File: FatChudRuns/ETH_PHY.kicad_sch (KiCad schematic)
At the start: 1 part, among them U2 DP83848I

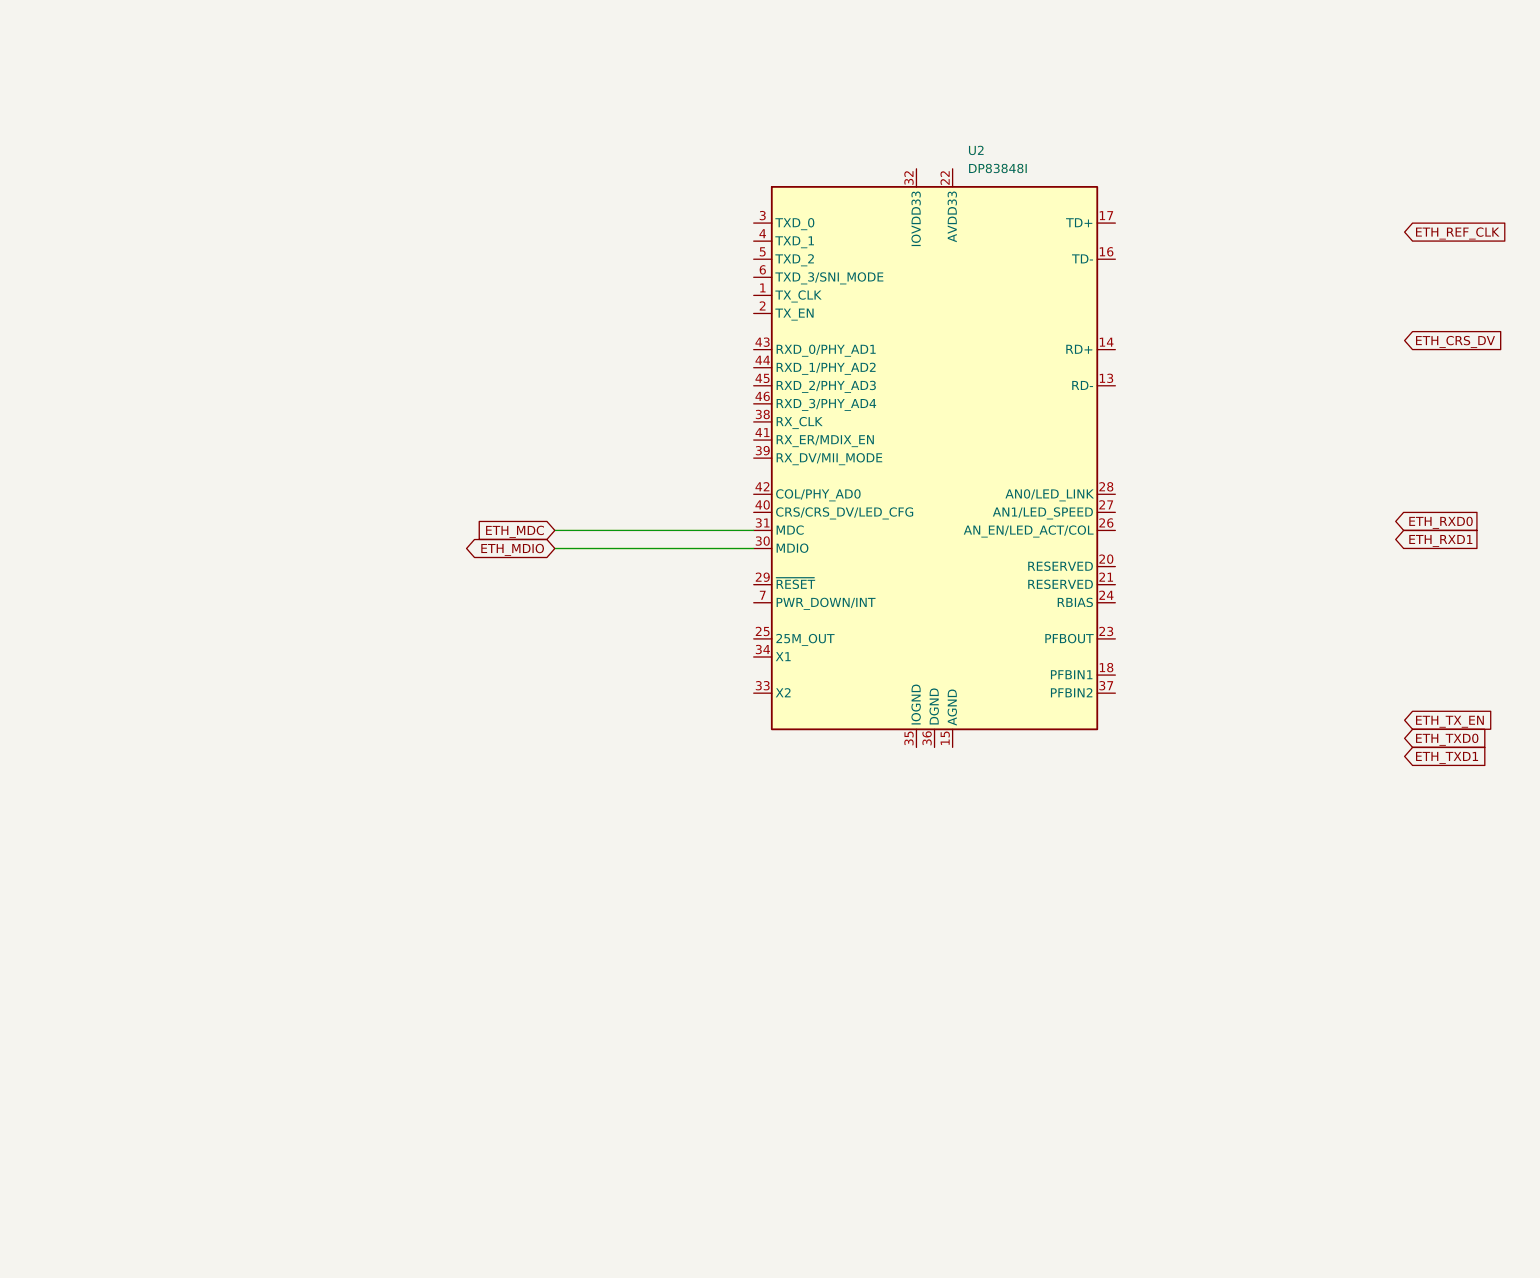
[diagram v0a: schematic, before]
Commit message: connected phy to uC and added strapping options
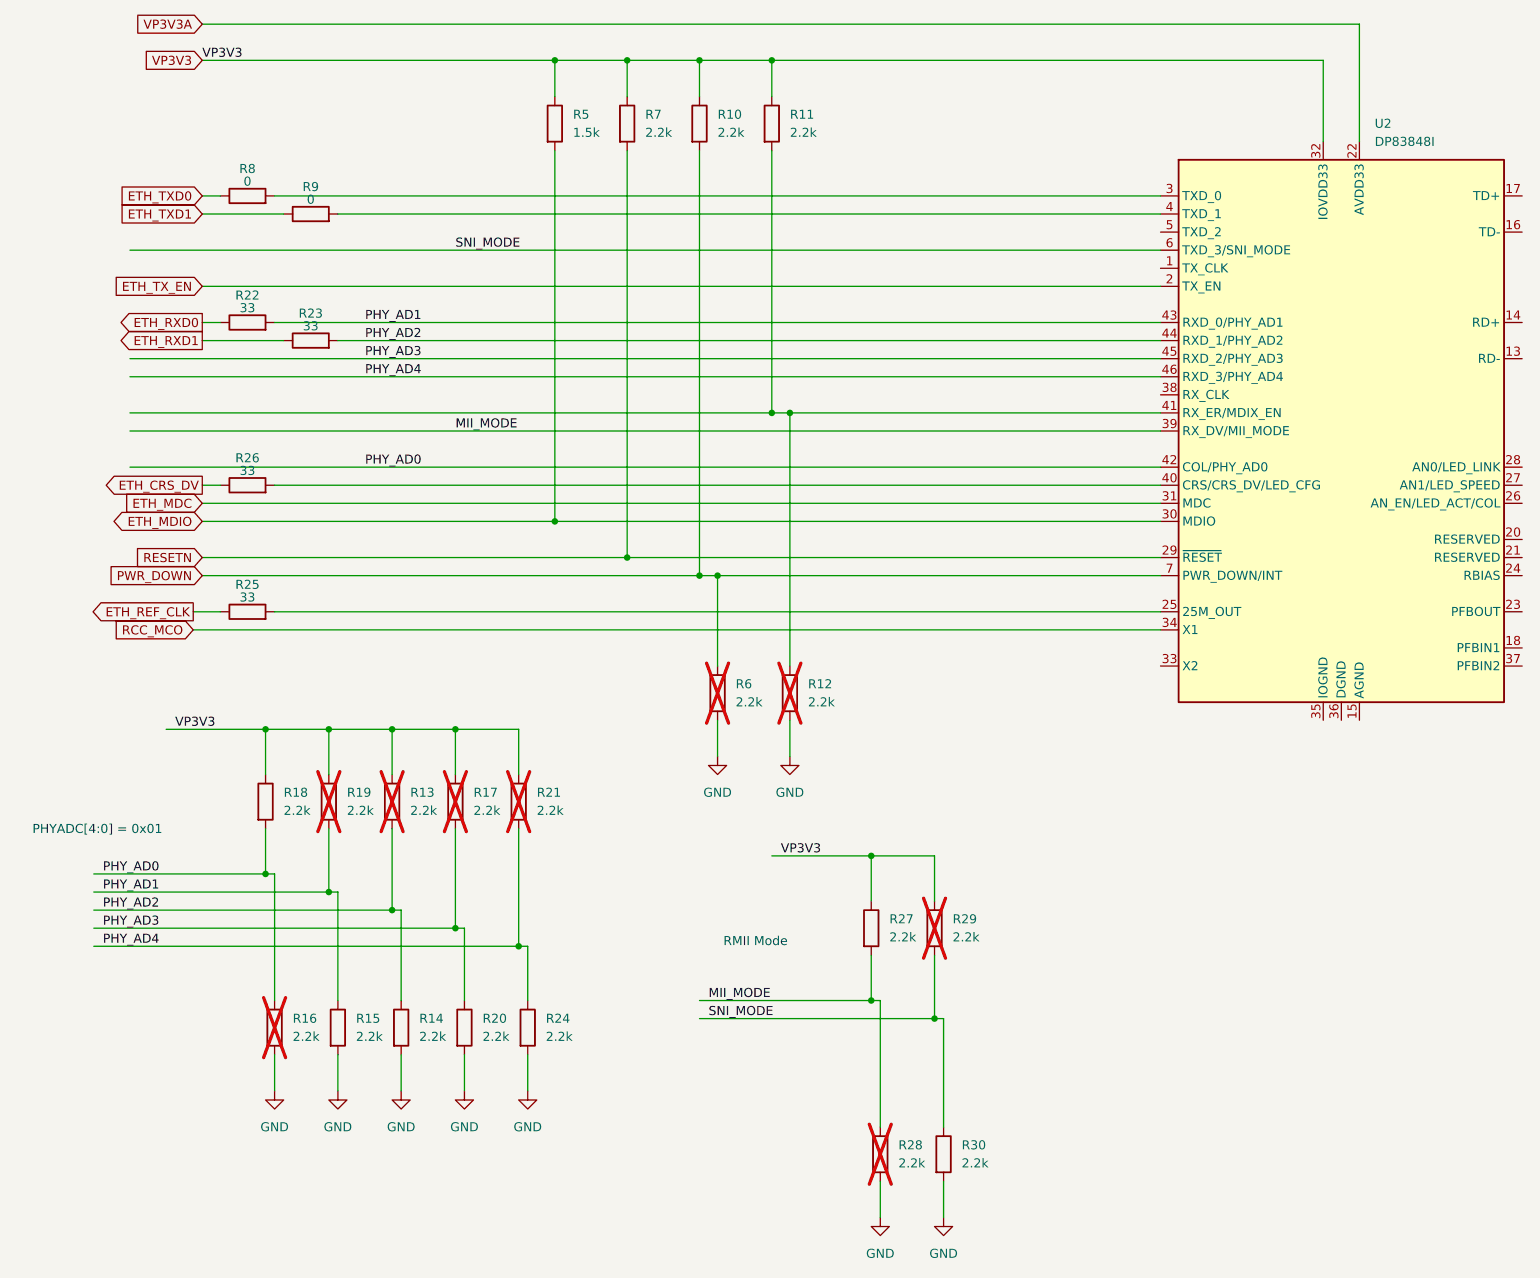
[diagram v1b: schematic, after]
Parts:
- added R10, R11, R12, R13, R14, R15, R16, R17, R18, R19, R20, R21, R24, R27, R28, R29, R30, R6, R7: 2.2k, Resistor_SMD:R_0603_1608Metric, symbol Device:R
- added R22, R23, R25, R26: 33, Resistor_SMD:R_0603_1608Metric, symbol Device:R
- added R5: 1.5k, Resistor_SMD:R_0603_1608Metric, symbol Device:R
- added R8, R9: 0, Resistor_SMD:R_0603_1608Metric, symbol Device:R
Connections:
- net ETH_CRS_DV: now also R26.1
- net ETH_MDIO: now also R5.2
- net ETH_REF_CLK: now also R25.1
- net ETH_RXD0: now also R22.1
- net ETH_RXD1: now also R23.1
- net ETH_TXD0: now also R8.1
- net ETH_TXD1: now also R9.1
- net ETH_TX_EN: now also U2.2 (TX_EN)
- net VP3V3A: now reaches U2.22 (AVDD33)
- net at U2.25 (25M_OUT): now also R25.2
- net RESETN: now reaches U2.29 (~{RESET})
- net RESETN: now also R7.2
- net at U2.3 (TXD_0): now also R8.2
- net VP3V3: now reaches U2.32 (IOVDD33), U2.48 (IOVDD33)
- net VP3V3: now also R10.1, R11.1, R13.1, R17.1, R18.1, R19.1, R21.1, R27.1, R29.1, R5.1, R7.1
- net RCC_MCO: now reaches U2.34 (X1)
- net MII_MODE: now reaches U2.39 (RX_DV/MII_MODE)
- net MII_MODE: now also R27.2, R28.1
- net at U2.4 (TXD_1): now also R9.2
- net at U2.40 (CRS/CRS_DV/LED_CFG): now also R26.2
- net at U2.41 (RX_ER/MDIX_EN): now also R11.2, R12.1
- net PHY_AD0: now reaches U2.42 (COL/PHY_AD0)
- net PHY_AD0: now also R16.1, R18.2
- net PHY_AD1: now reaches U2.43 (RXD_0/PHY_AD1)
- net PHY_AD1: now also R15.1, R19.2, R22.2
- net PHY_AD2: now reaches U2.44 (RXD_1/PHY_AD2)
- net PHY_AD2: now also R13.2, R14.1, R23.2
- net PHY_AD3: now reaches U2.45 (RXD_2/PHY_AD3)
- net PHY_AD3: now also R17.2, R20.1
- net PHY_AD4: now reaches U2.46 (RXD_3/PHY_AD4)
- net PHY_AD4: now also R21.2, R24.1
- net SNI_MODE: now reaches U2.6 (TXD_3/SNI_MODE)
- net SNI_MODE: now also R29.2, R30.1
- net PWR_DOWN: now reaches U2.7 (PWR_DOWN/INT)
- net PWR_DOWN: now also R10.2, R6.1
- new net GND: R12.2, R14.2, R15.2, R16.2, R20.2, R24.2, R28.2, R30.2, R6.2
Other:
- note added: "PHYADC[4:0] = 0x01"
- note added: "RMII Mode"
- moved on the sheet: U2

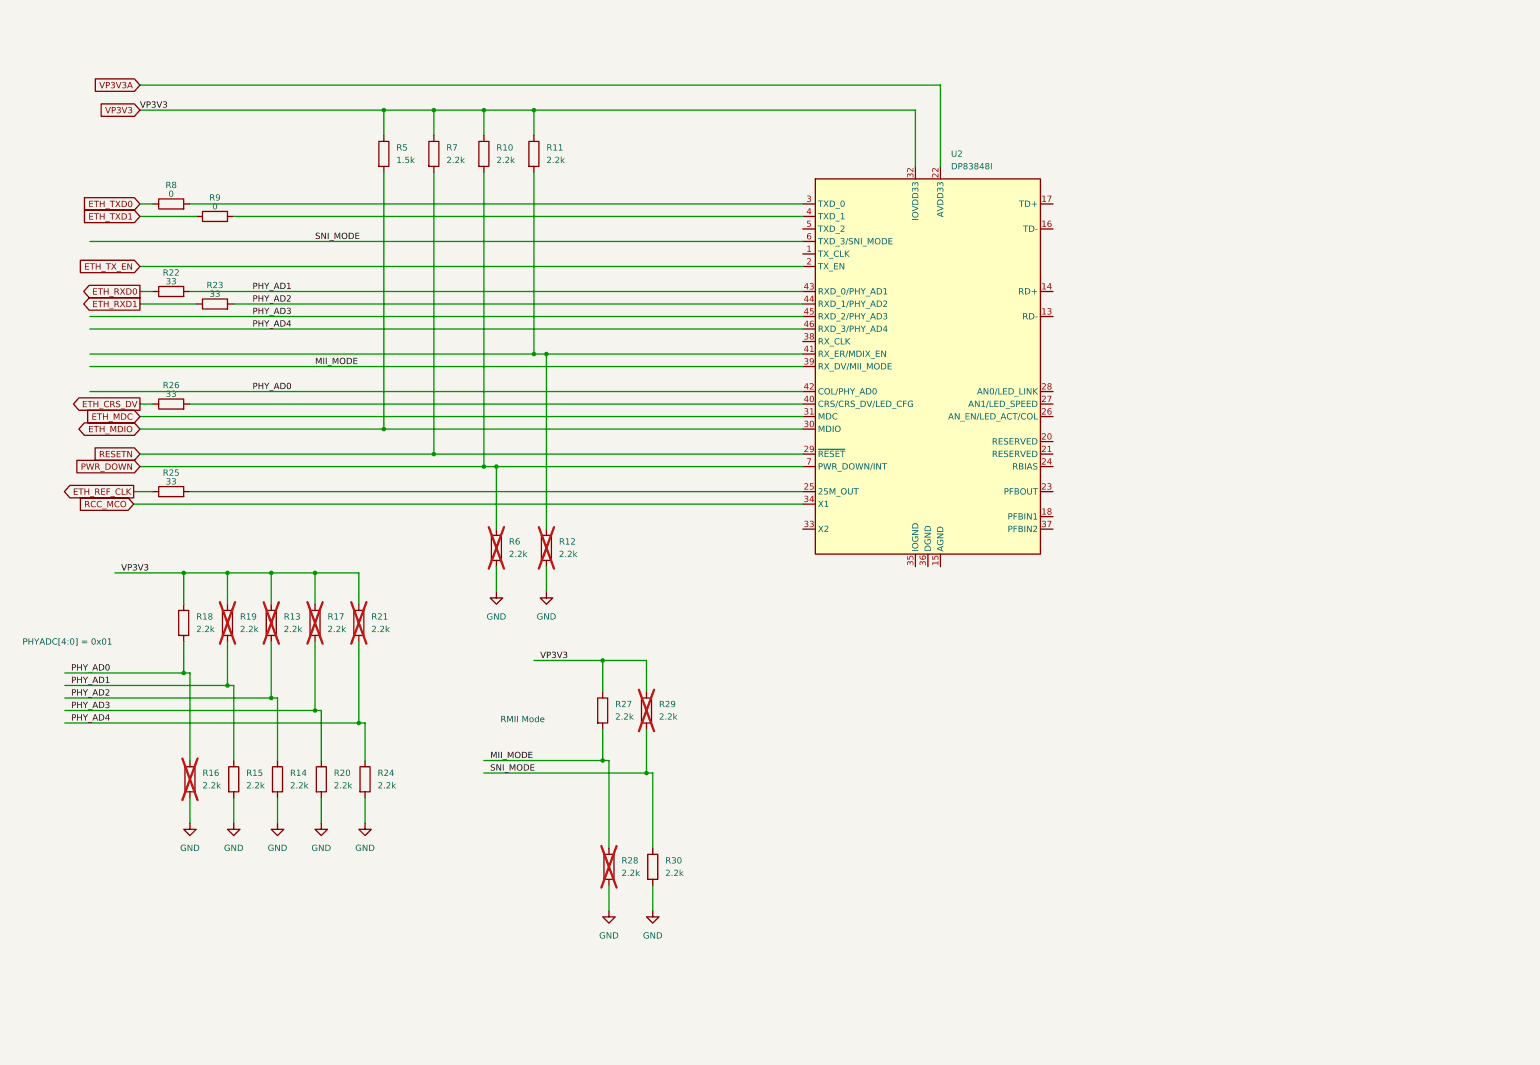
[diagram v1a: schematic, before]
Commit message: added filters and decoup caps, updated series term
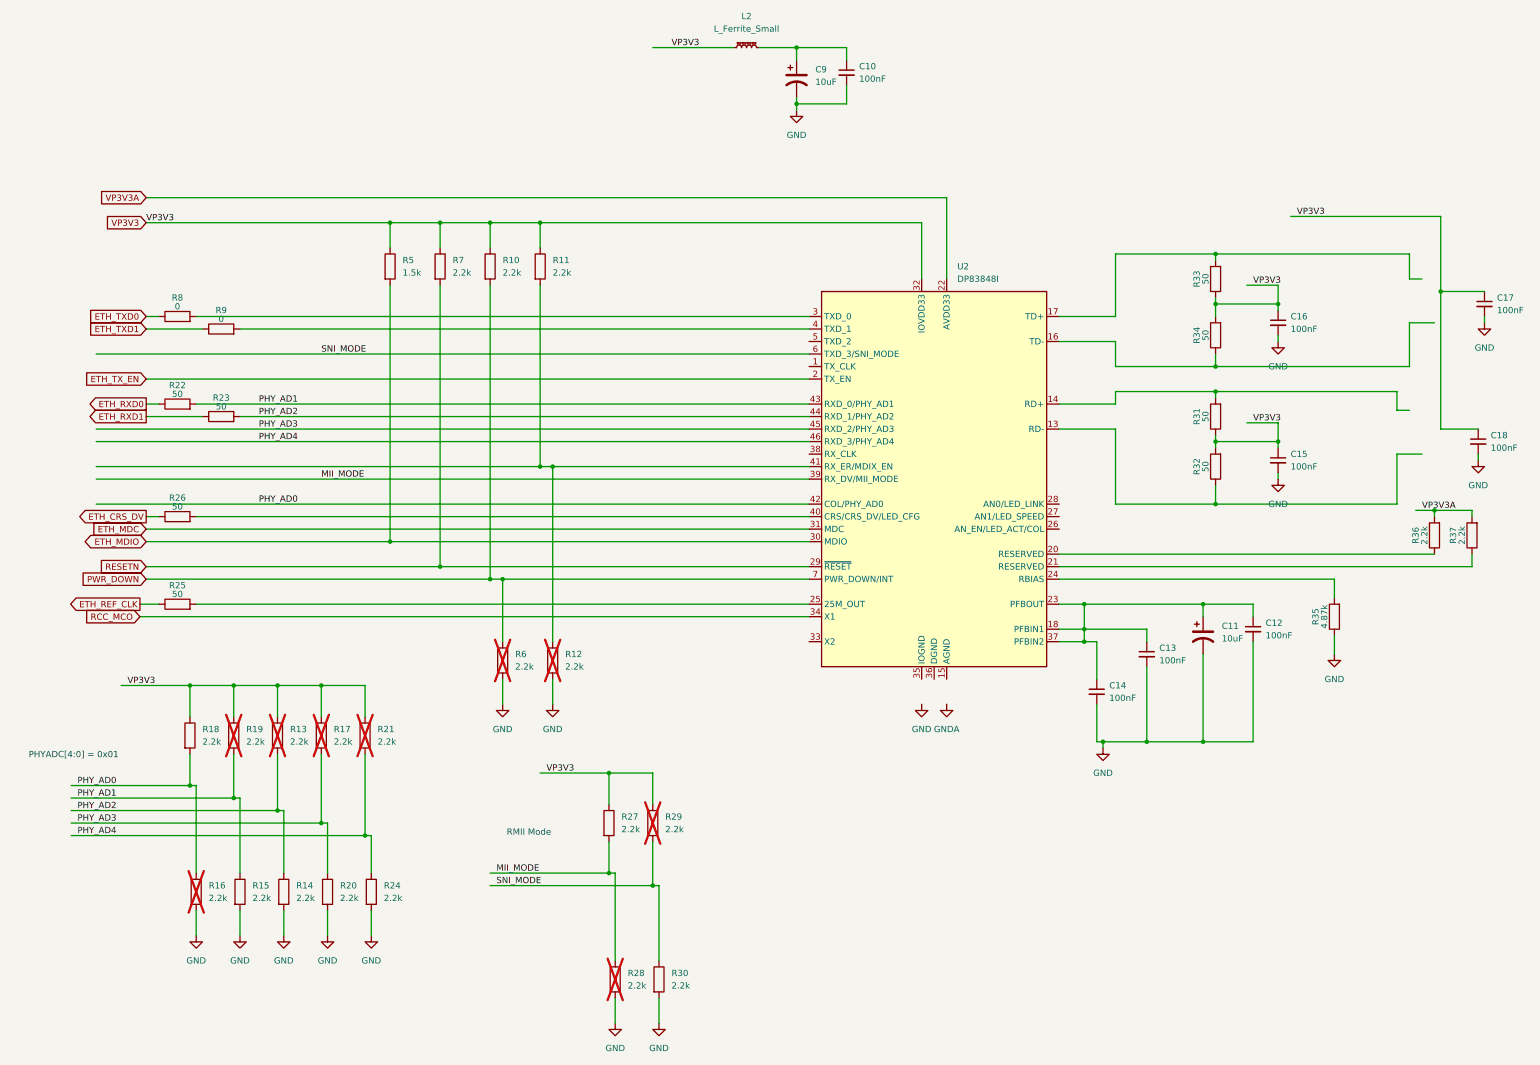
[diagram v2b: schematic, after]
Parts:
- added C10, C12, C13, C14, C15, C16, C17, C18: 100nF, symbol Device:C_Small
- added C11, C9: 10uF, symbol Device:C_Polarized_US
- added L2: L_Ferrite_Small, symbol Device:L_Ferrite_Small
- added R31, R32, R33, R34: 50, Resistor_SMD:R_0603_1608Metric, symbol Device:R
- added R35: 4.87k, Resistor_SMD:R_0603_1608Metric, symbol Device:R
- added R36, R37: 2.2k, Resistor_SMD:R_0603_1608Metric, symbol Device:R
- R22, R23, R25, R26: value 33 -> 50
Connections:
- net GND: now also C10.2, C11.2, C12.2, C13.2, C14.2, C15.2, C16.2, C17.2, C18.2, C9.2, R35.1
- net VP3V3: now also C15.1, C16.1, C17.1, C18.1, L2.1, R31.1, R32.2, R33.1, R34.2
- net VP3V3A: now also R36.2, R37.2
- net at U2.13 (RD-): now also R32.1
- net at U2.14 (RD+): now also R31.2
- net at U2.16 (TD-): now also R34.1
- net at U2.17 (TD+): now also R33.2
- net at U2.18 (PFBIN1): now also U2.23 (PFBOUT), U2.37 (PFBIN2), C11.1, C12.1, C13.1, C14.1
- net at U2.20 (RESERVED): now also R36.1
- net at U2.21 (RESERVED): now also R37.1
- net at U2.24 (RBIAS): now also R35.2
- new net: C10.1, C9.1, L2.2
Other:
- moved on the sheet: R10, R11, R12, R13, R14, R15, R16, R17, R18, R19, R20, R21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
